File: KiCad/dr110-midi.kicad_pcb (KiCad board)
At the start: 2 copper layers, 22 parts, among them J1 Conn_01x12_Male, J2 Conn_01x02_Male, Q1 BC547, Q2 BC547, Q3 BC547, Q4 BC547, Q5 BC547, Q6 BC547, Q7 BC547, U1 6N138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

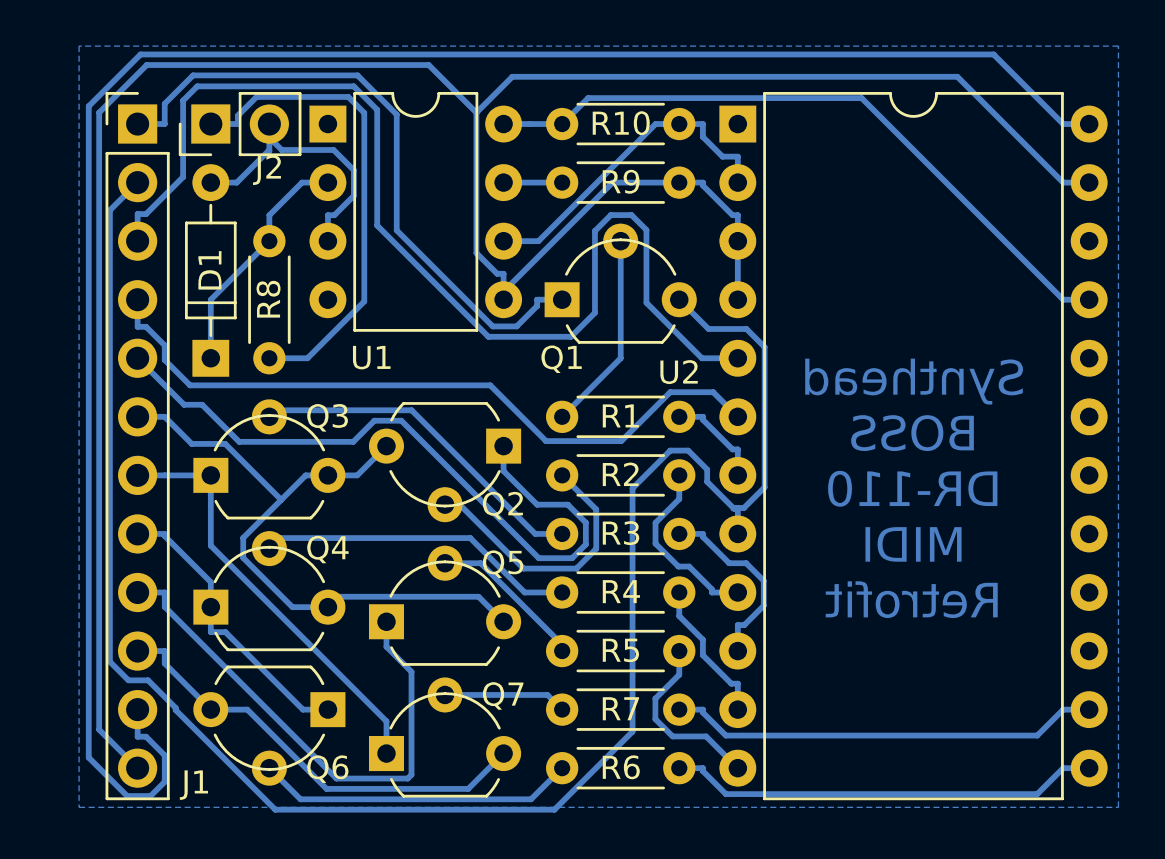
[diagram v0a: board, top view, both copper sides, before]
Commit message: Fix key matrix transistor pinouts.
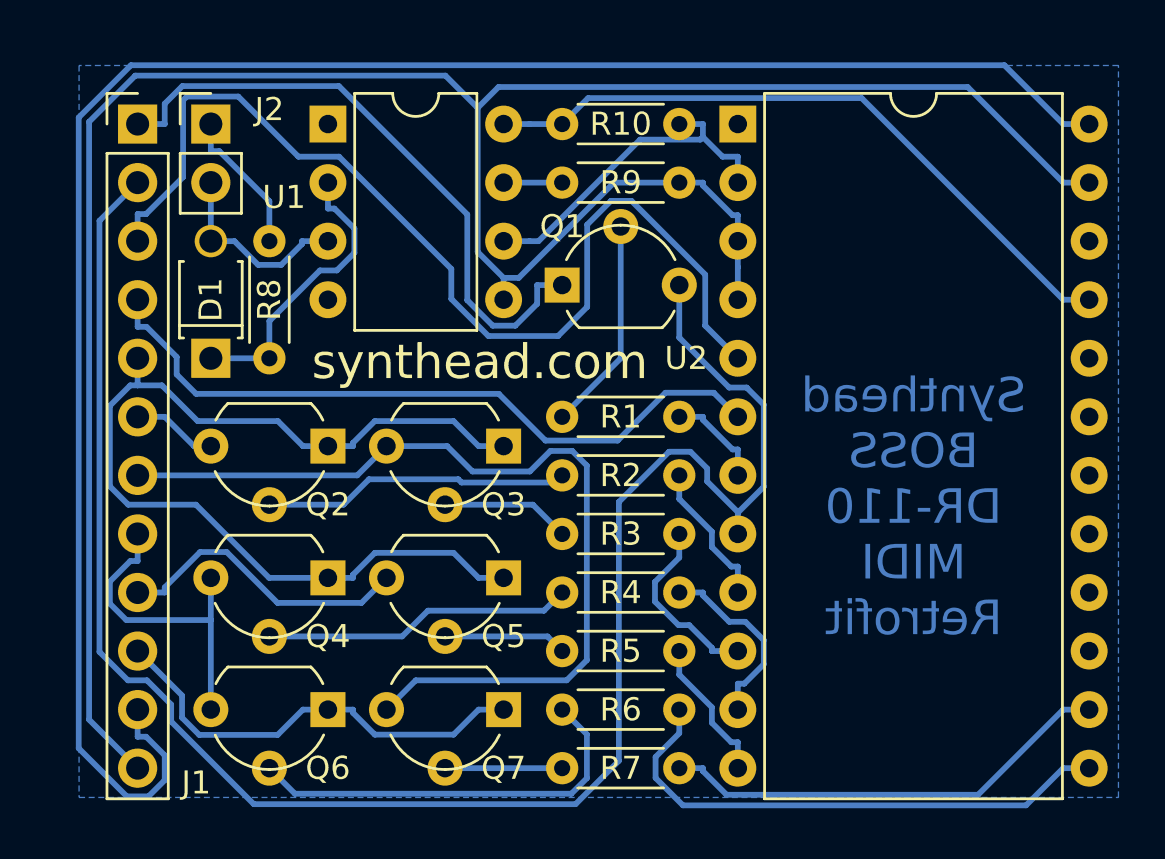
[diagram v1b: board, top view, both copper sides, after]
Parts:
- D1: footprint Diodes_THT:D_DO-35_SOD27_P7.62mm_Horizontal -> Diodes_THT:D_T-1_P5.08mm_Horizontal
- moved Q3 12.8 mm to (144.8, 97.2), turned to 180 degrees
- moved Q2 7.62 mm to (137.2, 97.2)
- moved Q5 5.43 mm to (144.8, 102.9), turned to 180 degrees
- moved Q7 5.43 mm to (144.8, 108.6), turned to 180 degrees
- moved Q4 5.24 mm to (137.2, 102.9), turned to 180 degrees
- moved R8 5.08 mm to (134.6, 93.3), turned to 90 degrees
- moved R6 2.54 mm to (147.3, 108.6)
- moved R7 2.54 mm to (147.3, 111.1)
- moved Q1 0.64 mm to (147.3, 90.2)
- turned J2 to 0 degrees
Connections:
- Q3 pad 1: MATRIX_3 -> MATRIX_1
- Q3 pad 3: MATRIX_2 -> MATRIX_3
- Q4 pad 1: MATRIX_4 -> MATRIX_1
- Q4 pad 3: MATRIX_2 -> MATRIX_4
- Q5 pad 1: MATRIX_5 -> MATRIX_1
- Q5 pad 3: MATRIX_2 -> MATRIX_5
- Q6 pad 1: MATRIX_4 -> MATRIX_6
- Q6 pad 3: MATRIX_6 -> MATRIX_4
- Q7 pad 1: MATRIX_3 -> MATRIX_6
- Q7 pad 3: MATRIX_6 -> MATRIX_3
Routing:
- net MATRIX_2: track 29.3 -> 3.70 mm
- net MATRIX_3: track 18.4 -> 39.1 mm
- net MIDI_IN_4: track 21.0 -> 6.35 mm
- net MATRIX_1: track 30.6 -> 43.9 mm
- net MATRIX_5: track 22.7 -> 13.0 mm
- net Net-(Q3-Pad2): track 15.0 -> 5.61 mm
- net Net-(R6-Pad2): track 18.8 -> 23.4 mm
- net Net-(Q6-Pad2): track 13.8 -> 17.9 mm
- net MIDI_IN_5: track 12.2 -> 8.55 mm
- net START: track 47.6 -> 45.0 mm
- net Net-(D1-Pad1): track 10.4 -> 12.8 mm
- net Net-(R4-Pad2): track 6.30 -> 8.24 mm
- net Net-(R2-Pad2): track 7.92 -> 6.30 mm
- net Net-(R5-Pad2): track 7.84 -> 6.30 mm
- net Net-(Q2-Pad2): track 11.9 -> 13.3 mm
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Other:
- board text added: "synthead.com"

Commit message: Add silkscreen text for connection pinouts.
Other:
- board text added: "6V"
- board text added: "CI"
- board text added: "CO"
- board text added: "GD"
- board text added: "I4"
- board text added: "I5"
- board text added: "M1"
- board text added: "M2"
- board text added: "M3"
- board text added: "M4"
- board text added: "M5"
- board text added: "M6"
- board text added: "SP"
- board text added: "ST"
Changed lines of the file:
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@@
   (general
     (thickness 1.6)
-    (drawings 2)
+    (drawings 16)
     (tracks 274)
     (zones 0)
@@
       (outputformat 4)
       (mirror true)
-      (drillshape 1)
+      (drillshape 0)
       (scaleselection 1)
       (outputdirectory "rendered/"))
@@
     (descr "8-lead though-hole mounted DIP package, row spacing 7.62 mm (300 mils)")
     (tags "THT DIP DIL PDIP 2.54mm 7.62mm 300mil")
-    (fp_text reference U1 (at -1.905 3.175) (layer F.SilkS)
+    (fp_text reference U1 (at 0 -1.905) (layer F.SilkS)
       (effects (font (size 1 1) (thickness 0.15)))
     )
@@
   (module dr110-midi:ProMicro (layer F.Cu)
     (at 162.56 95.885)
-    (fp_text reference U2 (at -9.859501 -2.54) (layer F.SilkS)
+    (fp_text reference U2 (at -9.859501 -14.605) (layer F.SilkS)
       (effects (font (size 1 1) (thickness 0.15)))
     )
@@
     (descr "Through hole straight socket strip, 1x12, 2.54mm pitch, single row")
     (tags "Through hole socket strip THT 1x12 2.54mm single row")
-    (fp_text reference J1 (at 2.54 28.575) (layer F.SilkS)
+    (fp_text reference J1 (at 0 -1.905) (layer F.SilkS)
       (effects (font (size 1 1) (thickness 0.15)))
     )
@@
     (descr "Through hole straight socket strip, 1x02, 2.54mm pitch, single row")
     (tags "Through hole socket strip THT 1x02 2.54mm single row")
-    (fp_text reference J2 (at 2.54 -0.635 180) (layer F.SilkS)
+    (fp_text reference J2 (at 0 -1.905 180) (layer F.SilkS)
       (effects (font (size 1 1) (thickness 0.15)))
     )
@@
     )
   )
+  (gr_text I5 (at 133.35 85.725) (layer F.SilkS)
+    (effects (font (size 1 1) (thickness 0.15)) (justify left))
+  )
+  (gr_text I4 (at 133.35 83.185) (layer F.SilkS)
+    (effects (font (size 1 1) (thickness 0.15)) (justify left))
+  )
+  (gr_text M6 (at 127.635 106.045) (layer F.SilkS)
+    (effects (font (size 1 1) (thickness 0.15)) (justify right))
+  )
+  (gr_text M5 (at 127.635 103.505) (layer F.SilkS)
+    (effects (font (size 1 1) (thickness 0.15)) (justify right))
+  )
+  (gr_text M4 (at 127.635 100.965) (layer F.SilkS)
+    (effects (font (size 1 1) (thickness 0.15)) (justify right))
+  )
+  (gr_text M3 (at 127.635 98.425) (layer F.SilkS)
+    (effects (font (size 1 1) (thickness 0.15)) (justify right))
+  )
+  (gr_text M2 (at 127.635 95.885) (layer F.SilkS)
+    (effects (font (size 1 1) (thickness 0.15)) (justify right))
+  )
+  (gr_text M1 (at 127.635 93.345) (layer F.SilkS)
+    (effects (font (size 1 1) (thickness 0.15)) (justify right))
+  )
+  (gr_text SP (at 127.635 90.805) (layer F.SilkS)
+    (effects (font (size 1 1) (thickness 0.15)) (justify right))
+  )
+  (gr_text ST (at 127.635 88.265) (layer F.SilkS)
+    (effects (font (size 1 1) (thickness 0.15)) (justify right))
+  )
+  (gr_text CO (at 127.635 85.725) (layer F.SilkS)
+    (effects (font (size 1 1) (thickness 0.15)) (justify right))
+  )
+  (gr_text CI (at 127.635 83.185) (layer F.SilkS)
+    (effects (font (size 1 1) (thickness 0.15)) (justify right))
+  )
+  (gr_text 6V (at 127.635 108.585) (layer F.SilkS)
+    (effects (font (size 1 1) (thickness 0.15)) (justify right))
+  )
+  (gr_text GD (at 127.635 111.125) (layer F.SilkS)
+    (effects (font (size 1 1) (thickness 0.15)) (justify right))
+  )
   (gr_text synthead.com (at 143.748923 93.509405) (layer F.SilkS)
